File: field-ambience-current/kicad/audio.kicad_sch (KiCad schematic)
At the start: 9 parts, among them J4 SWD 1.27mm (SWCLK/GND/SWDIO), SW11 Reset 6mm SMD, SW12 BOOTSEL 6mm SMD (DNP for THT-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, U1 Raspberry_Pi_Pico2 (RP2350)

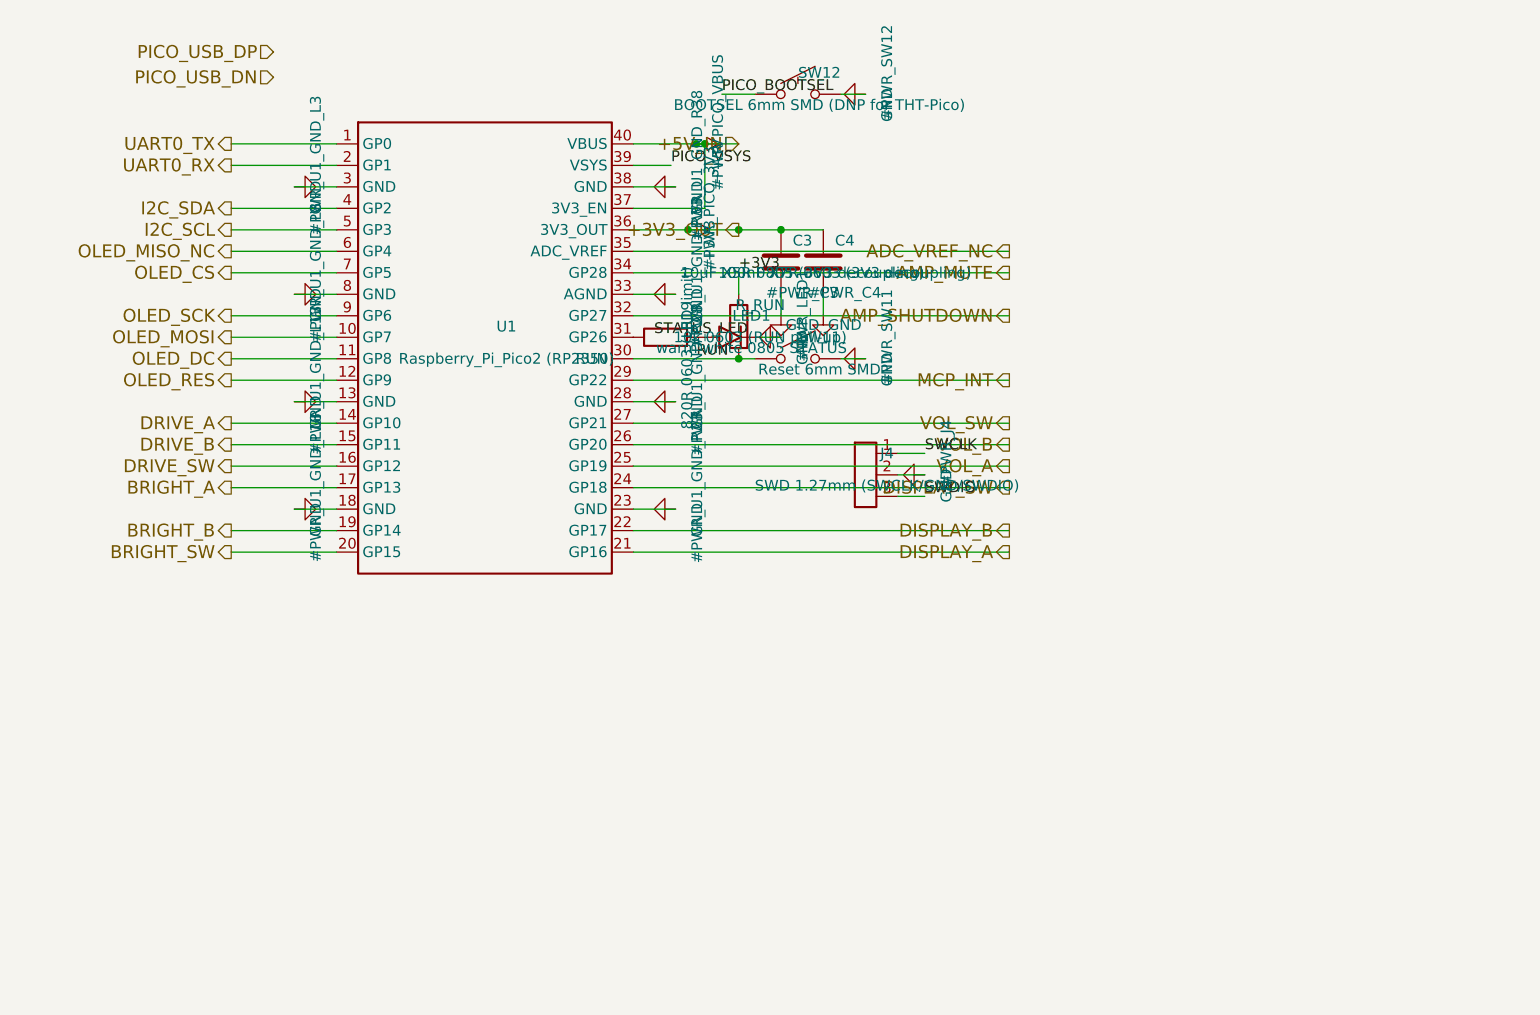
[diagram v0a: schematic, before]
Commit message: Add Sheet 6 (Audio) per SPEC v0.6 §8 + H2/M2/C2 Fixes
U3 PCM5102A (TSSOP-20, C107671) I²S DAC:
- Pin 1-3: I2S_LRCK/BCK/DOUT ← hier-inputs (von Sheet 7 Pi-Header später)
- 3-wire mode: SCK (pin 18) → GND (internal PLL aus BCK)
- FMT (8) → GND I²S mode, FLT (5) → GND, DEMP (6) → GND
- XSMT (7) → R_XSMT 10k pull-up zu +3V3 (un-muted by default)
- VCOM (14): C_VCOM 1µF filter, VNEG (11): C_VNEG 1µF filter
- CPVDD (13): C_CPVDD 10µF + 100nF (charge pump supply)
- DVDD (19): C8a 10µF + C8b 100nF (digital)
- AVDD (15): via FB1 BLM18AG601 + C7a 10µF + C7b 100nF (v0.6 M2 Fix)
- VOUTL (9), VOUTR (16) → coupling zu PAM8403

FB1 BLM18AG601 (C19330) Ferrit-Bead zwischen +3V3 und AVDD-Pin.

U4 PAM8403 (SOP-16, C17337) Class-D Stereo Amp:
- VDD (1, 15, 16) → +5V mit C9 10µF + C9b 100nF lokal (v0.6 H2 Fix)
- SHDN (3) ← AMP_SHUTDOWN von Pico GP27 (v0.6 C2 Fix Pop-Suppression)
- MUTE (4) ← AMP_MUTE von Pico GP28 (v0.6 C2 Fix)
- INL+ (5) ← C_in_L 1µF DC-block + R_VOL_L 10k series ← PCM_VOUTL
- INR+ (7) ← C_in_R 1µF DC-block + R_VOL_R 10k series ← PCM_VOUTR
- INL-/INR- (6/8) → GND (single-ended, internal bias)
- OUTL+/- (9/10) → J6 Speaker L (PUI AS04008PS 4Ω/4W BTL)
- OUTR+/- (11/12) → J7 Speaker R (PUI AS04008PS 4Ω/4W BTL)

Note: PAM8403 pinout variiert zwischen Herstellern. Vor PCB-Layout
gegen tatsächliches Datasheet von JLC-stockable PAM8403 (C17337)
verifizieren. KiCad-Symbol nutzt logisches Pinout.

Root sheet: Audio-Sheet bei (230, 200) size (60, 50) mit 5 input pins.
Pico-Sheet bekommt AMP_SHUTDOWN/AMP_MUTE outputs auf linker Seite.
Label-bridges für AMP_SHDN, AMP_MUTE, I2S_BCK/LRCK/DOUT.
I2S-Signale bleiben momentan dangling (Sheet 7 Pi-Header noch nicht
implementiert).

Analyzer: 0 functional errors (3 VM-001 false positives unverändert).
24 warnings, 81 components, 86 nets total. U3+U4 pin_nets verifiziert.
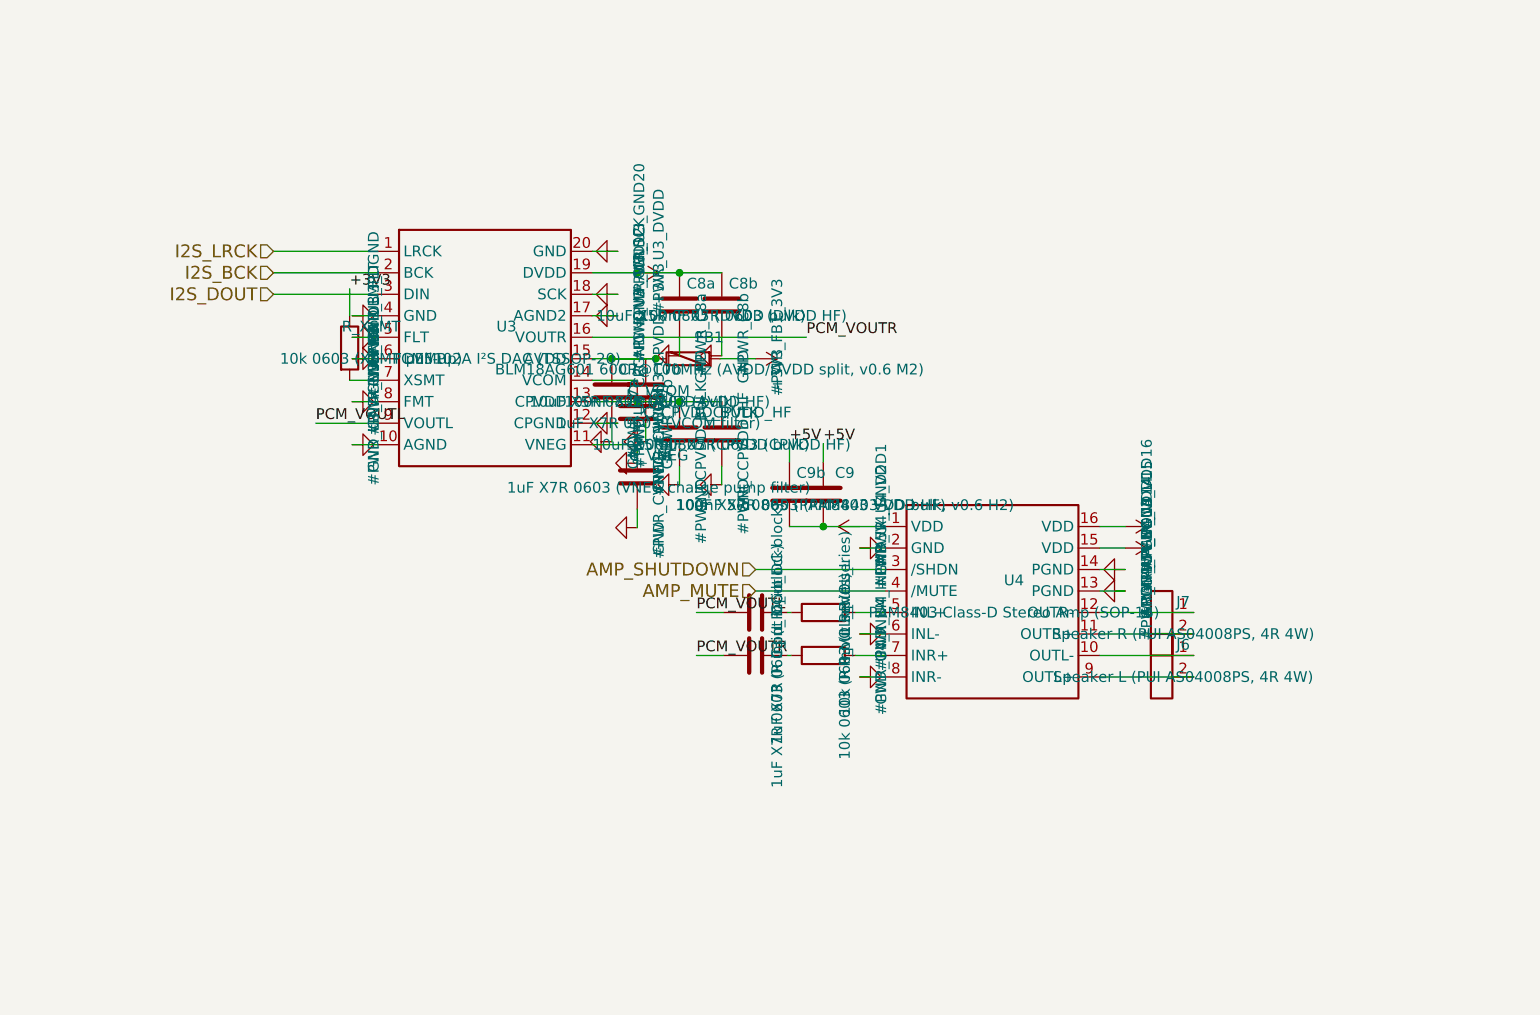
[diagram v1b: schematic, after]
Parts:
- removed C3: 10uF X5R 0805 (3V3 decoupling), Capacitor_SMD:C_0805_2012Metric, symbol Device:C
- removed C4: 100nF X7R 0603 (3V3 decoupling), Capacitor_SMD:C_0603_1608Metric, symbol Device:C
- removed J4: SWD 1.27mm (SWCLK/GND/SWDIO), Connector_PinHeader_1.27mm:PinHeader_1x03_P1.27mm_Vertical, symbol Connector:Conn_01x03
- removed LED1: warm white 0805 STATUS, LED_SMD:LED_0805_2012Metric, symbol Device:LED
- removed R19: 820R 0603 (LED limit), Resistor_SMD:R_0603_1608Metric, symbol Device:R
- removed R_RUN: 10k 0603 (RUN pull-up), Resistor_SMD:R_0603_1608Metric, symbol Device:R
- removed SW11: Reset 6mm SMD, Button_Switch_SMD:SW_SPST_TL3342, symbol Switch:SW_Push
- removed SW12: BOOTSEL 6mm SMD (DNP for THT-Pico), Button_Switch_SMD:SW_SPST_TL3342, symbol Switch:SW_Push
- removed U1: Raspberry_Pi_Pico2 (RP2350), MCU_Module:RPi_Pico_SMD_TH, symbol MCU:Pico2
- added C7a: 10uF X5R 0805 (AVDD bulk), Capacitor_SMD:C_0805_2012Metric, symbol Device:C
- added C7b: 100nF X7R 0603 (AVDD HF), Capacitor_SMD:C_0603_1608Metric, symbol Device:C
- added C8a: 10uF X5R 0805 (DVDD bulk), Capacitor_SMD:C_0805_2012Metric, symbol Device:C
- added C8b: 100nF X7R 0603 (DVDD HF), Capacitor_SMD:C_0603_1608Metric, symbol Device:C
- added C9: 10uF X5R 0805 (PAM8403 VDD bulk, v0.6 H2), Capacitor_SMD:C_0805_2012Metric, symbol Device:C
- added C9b: 100nF X7R 0603 (PAM8403 VDD HF), Capacitor_SMD:C_0603_1608Metric, symbol Device:C
- added C_CPVDD_BULK: 10uF X5R 0805 (CPVDD bulk), Capacitor_SMD:C_0805_2012Metric, symbol Device:C
- added C_CPVDD_HF: 100nF X7R 0603 (CPVDD HF), Capacitor_SMD:C_0603_1608Metric, symbol Device:C
- added C_VCOM: 1uF X7R 0603 (VCOM filter), Capacitor_SMD:C_0603_1608Metric, symbol Device:C
- added C_VNEG: 1uF X7R 0603 (VNEG charge pump filter), Capacitor_SMD:C_0603_1608Metric, symbol Device:C
- added C_in_L: 1uF X7R 0603 (L input DC-block), Capacitor_SMD:C_0603_1608Metric, symbol Device:C
- added C_in_R: 1uF X7R 0603 (R input DC-block), Capacitor_SMD:C_0603_1608Metric, symbol Device:C
- added FB1: BLM18AG601 600R@100MHz (AVDD/DVDD split, v0.6 M2), Inductor_SMD:L_0603_1608Metric, symbol Device:Ferrite_Bead
- added J6: Speaker L (PUI AS04008PS, 4R 4W), Connector_PinHeader_2.54mm:PinHeader_1x02_P2.54mm_Vertical, symbol Connector:Conn_01x02
- added J7: Speaker R (PUI AS04008PS, 4R 4W), Connector_PinHeader_2.54mm:PinHeader_1x02_P2.54mm_Vertical, symbol Connector:Conn_01x02
- added R_VOL_L: 10k 0603 (L input series), Resistor_SMD:R_0603_1608Metric, symbol Device:R
- added R_VOL_R: 10k 0603 (R input series), Resistor_SMD:R_0603_1608Metric, symbol Device:R
- added R_XSMT: 10k 0603 (XSMT pull-up), Resistor_SMD:R_0603_1608Metric, symbol Device:R
- added U3: PCM5102A I²S DAC (TSSOP-20), Package_SO:TSSOP-20_4.4x6.5mm_P0.65mm, symbol Audio:PCM5102A
- added U4: PAM8403 Class-D Stereo Amp (SOP-16), Package_SO:SOIC-16_3.9x9.9mm_P1.27mm, symbol Audio:PAM8403
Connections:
- net +3V3: now also C8a.1, C8b.1, C_CPVDD_BULK.1, C_CPVDD_HF.1, FB1.1, R_XSMT.1, U3.13 (CPVDD), U3.19 (DVDD)
- net +5V: now also C9.1, C9.2, C9b.1, C9b.2, U4.1 (VDD), U4.15 (VDD), U4.16 (VDD)
- net AMP_MUTE: now also U4.4 (/MUTE)
- net AMP_SHUTDOWN: now also U4.3 (/SHDN)
- net GND: now also C7a.2, C7b.2, C8a.2, C8b.2, C_CPVDD_BULK.2, C_CPVDD_HF.2, C_VCOM.2, C_VNEG.1, C_VNEG.2, U3.10 (AGND), U3.11 (VNEG), U3.12 (CPGND), U3.17 (AGND2), U3.18 (SCK), U3.20 (GND), U3.4 (GND), U3.5 (FLT), U3.6 (DEMP), U3.8 (FMT), U4.13 (PGND), U4.14 (PGND), U4.2 (GND), U4.6 (INL-), U4.8 (INR-)
- new net: R_XSMT.2, U3.7 (XSMT)
- new net: J6.1 (Pin_1), U4.10 (OUTL-)
- new net: J7.2 (Pin_2), U4.11 (OUTR+)
- new net: J7.1 (Pin_1), U4.12 (OUTR-)
- new net: R_VOL_L.2, U4.5 (INL+)
- new net: R_VOL_R.2, U4.7 (INR+)
- new net: J6.2 (Pin_2), U4.9 (OUTL+)
- new net: C_VCOM.1, U3.14 (VCOM)
- new net: C7a.1, C7b.1, FB1.2, U3.15 (AVDD)
- new net: C_in_R.2, R_VOL_R.1
- new net: C_in_L.2, R_VOL_L.1
- new net I2S_BCK: U3.2 (BCK)
- new net I2S_DOUT: U3.3 (DIN)
- new net I2S_LRCK: U3.1 (LRCK)
- new net PCM_VOUTL: C_in_L.1, U3.9 (VOUTL)
- new net PCM_VOUTR: C_in_R.1, U3.16 (VOUTR)
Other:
- title: Field Ambience PCB — Sheet 2: Pico 2 (RP2350) -> Field Ambience PCB — Sheet 6: Audio (PCM5102A + PAM8403)
